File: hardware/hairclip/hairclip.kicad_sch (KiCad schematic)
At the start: 2 parts, among them U1 NRF52840-CKAA-R

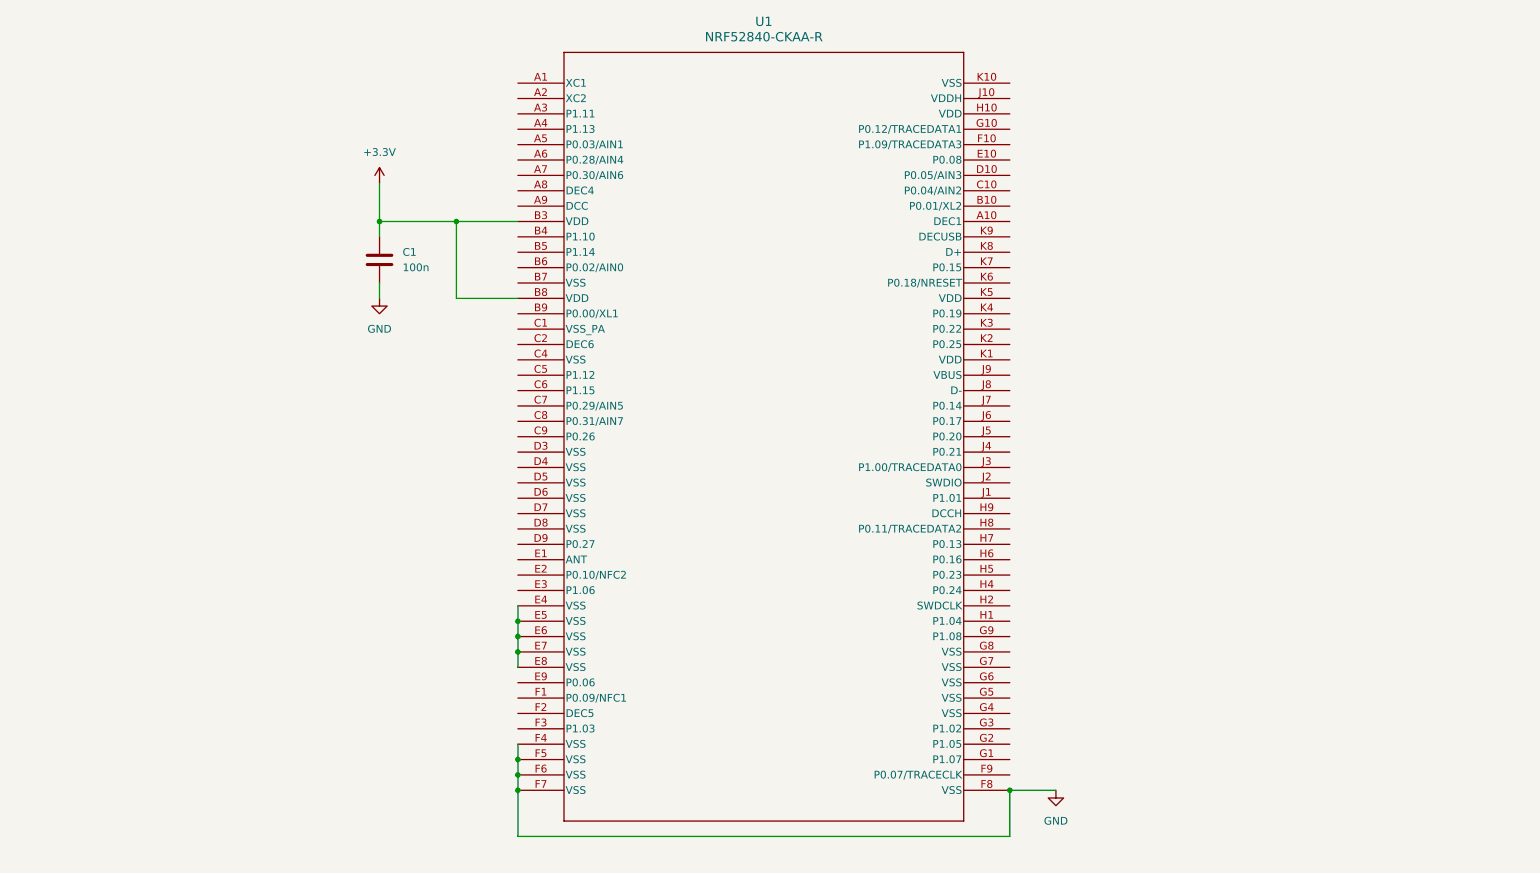
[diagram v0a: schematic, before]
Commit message: add low speed oscillator
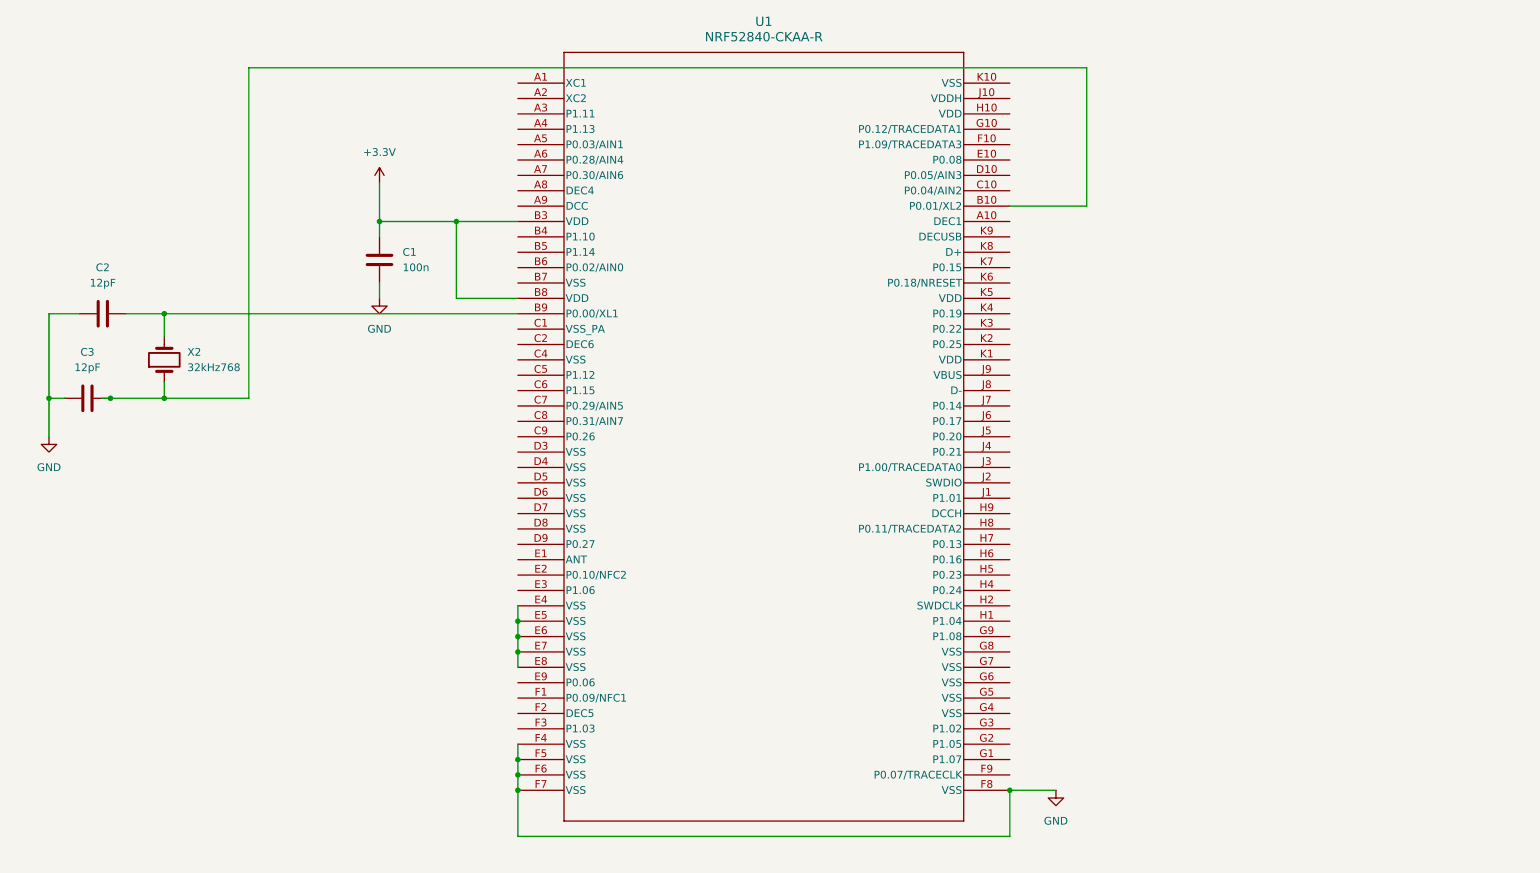
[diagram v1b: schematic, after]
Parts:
- added C2, C3: 12pF, symbol Device:C
- added X2: 32kHz768, symbol Device:Crystal
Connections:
- net GND: now also C2.1, C3.1
- net at U1.B10 (P0.01/XL2): now also C3.2, X2.1
- net at U1.B9 (P0.00/XL1): now also C2.2, X2.2

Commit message: Add high speed oscillator, antenna, LED, JTAG, Voltage regulator
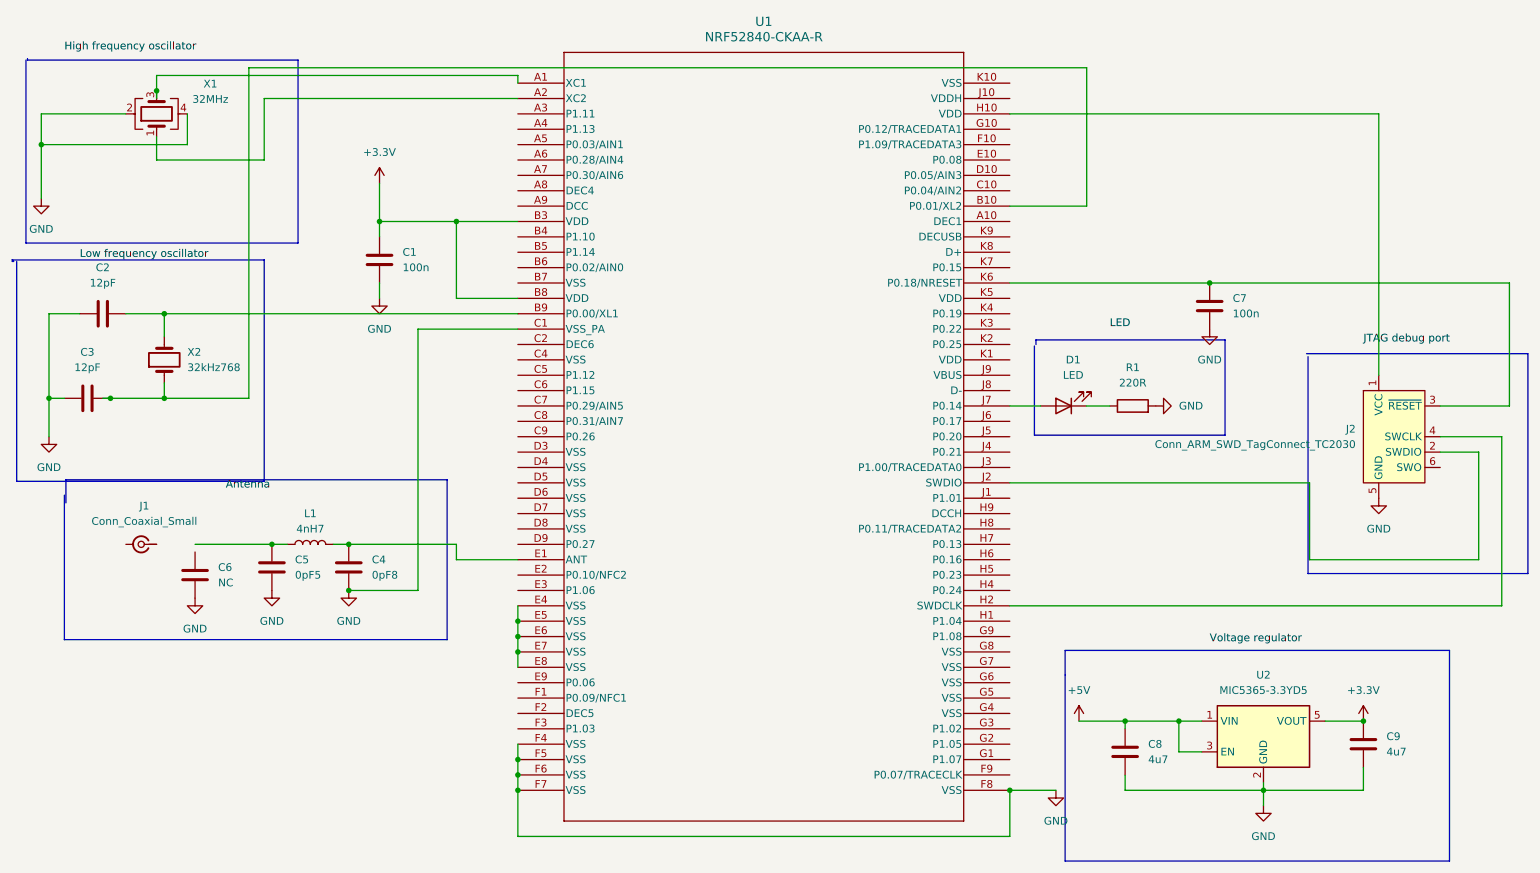
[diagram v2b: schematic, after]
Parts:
- added C4: 0pF8, symbol Device:C
- added C5: 0pF5, symbol Device:C
- added C6: NC, symbol Device:C
- added C7: 100n, symbol Device:C
- added C8, C9: 4u7, symbol Device:C
- added D1: LED, symbol Device:LED
- added J1: Conn_Coaxial_Small, symbol Connector:Conn_Coaxial_Small
- added J2: Conn_ARM_SWD_TagConnect_TC2030, Connector_PinHeader_1.27mm:PinHeader_2x05_P1.27mm_Vertical_SMD, symbol Connector:Conn_ARM_SWD_TagConnect_TC2030
- added L1: 4nH7, symbol Device:L
- added R1: 220R, symbol Device:R
- added U2: MIC5365-3.3YD5, Package_TO_SOT_SMD:SOT-23-5, symbol Regulator_Linear:MIC5365-3.3YD5
- added X1: 32MHz, symbol Device:Crystal_GND24
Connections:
- net +3.3V: now also C9.1, U2.5 (VOUT)
- net GND: now also U1.C1 (VSS_PA), C4.2, C5.2, C6.2, C7.2, C8.2, C9.2, J2.5 (GND), R1.2, U2.2 (GND), X1.2, X1.4
- net at U1.A1 (XC1): now also X1.3
- net at U1.A2 (XC2): now also X1.1
- net at U1.E1 (ANT): now also C4.1, L1.2
- net at U1.H10 (VDD): now also J2.1 (VCC)
- net at U1.H2 (SWDCLK): now also J2.4 (SWCLK)
- net at U1.J2 (SWDIO): now also J2.2 (SWDIO)
- net at U1.J7 (P0.14): now also D1.2 (A)
- net at U1.K6 (P0.18/NRESET): now also C7.1, J2.3 (~{RESET})
- new net: D1.1 (K), R1.1
- new net: C5.1, L1.1
- new net +5V: C8.1, U2.1 (VIN), U2.3 (EN)

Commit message: add initial pcb
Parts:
- C1: renamed from C3; footprint (none) -> Capacitor_SMD:C_0402_1005Metric
- C2: footprint (none) -> Capacitor_SMD:C_0402_1005Metric
- C3: renamed from C6; footprint (none) -> Capacitor_SMD:C_0402_1005Metric
- C4: renamed from C5; footprint (none) -> Capacitor_SMD:C_0402_1005Metric
- C5: renamed from C4; footprint (none) -> Capacitor_SMD:C_0402_1005Metric
- C6: renamed from C1; footprint (none) -> Capacitor_SMD:C_0402_1005Metric
- C7: renamed from C8; footprint (none) -> Capacitor_SMD:C_0805_2012Metric
- C8: renamed from C7; footprint (none) -> Capacitor_SMD:C_0402_1005Metric
- C9: footprint (none) -> Capacitor_SMD:C_0805_2012Metric
- D1: footprint (none) -> LED_SMD:LED_0201_0603Metric
- J1: footprint (none) -> Connector_Coaxial:U.FL_Hirose_U.FL-R-SMT-1_Vertical
- L1: footprint (none) -> Inductor_SMD:L_0402_1005Metric
- R1: footprint (none) -> Resistor_SMD:R_0402_1005Metric
- U1: footprint WLCSP94_3P5X3P6_NOR -> Package_DFN_QFN:Nordic_AQFN-73-1EP_7x7mm_P0.5mm
- X1, X2: footprint (none) -> Oscillator:Oscillator_SMD_Abracon_ASCO-4Pin_1.6x1.2mm
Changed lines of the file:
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@@
 		(dnp no)
 		(fields_autoplaced yes)
-		(property "Reference" "#PWR09"
+		(property "Reference" "#PWR014"
 			(at 241.3 116.84 0)
 			(effects
@@
 			(project "hairclip"
 				(path "/d641266f-28be-4124-8b00-4ae47c4ffb54"
-					(reference "#PWR09")
+					(reference "#PWR014")
 					(unit 1)
 				)
@@
 		(dnp no)
 		(fields_autoplaced yes)
-		(property "Reference" "#PWR06"
+		(property "Reference" "#PWR05"
 			(at 71.12 132.08 0)
 			(effects
@@
 			(project "hairclip"
 				(path "/d641266f-28be-4124-8b00-4ae47c4ffb54"
-					(reference "#PWR06")
+					(reference "#PWR05")
 					(unit 1)
 				)
@@
 		(dnp no)
 		(fields_autoplaced yes)
-		(property "Reference" "#PWR02"
+		(property "Reference" "#PWR07"
 			(at 76.2 83.82 0)
 			(effects
@@
 			(project "hairclip"
 				(path "/d641266f-28be-4124-8b00-4ae47c4ffb54"
-					(reference "#PWR02")
+					(reference "#PWR07")
 					(unit 1)
 				)
@@
 			)
 		)
-		(property "Footprint" ""
+		(property "Footprint" "Connector_Coaxial:U.FL_Hirose_U.FL-R-SMT-1_Vertical"
 			(at 36.83 118.11 0)
 			(effects
@@
 		(dnp no)
 		(fields_autoplaced yes)
-		(property "Reference" "C8"
+		(property "Reference" "C7"
 			(at 203.2 151.1299 0)
 			(effects
@@
 			)
 		)
-		(property "Footprint" ""
+		(property "Footprint" "Capacitor_SMD:C_0805_2012Metric"
 			(at 200.3552 156.21 0)
 			(effects
@@
 			(project "hairclip"
 				(path "/d641266f-28be-4124-8b00-4ae47c4ffb54"
-					(reference "C8")
+					(reference "C7")
 					(unit 1)
 				)
@@
 			)
 		)
-		(property "Footprint" "WLCSP94_3P5X3P6_NOR"
+		(property "Footprint" "Package_DFN_QFN:Nordic_AQFN-73-1EP_7x7mm_P0.5mm"
 			(at 99.06 41.91 0)
 			(effects
@@
 		(dnp no)
 		(fields_autoplaced yes)
-		(property "Reference" "C4"
+		(property "Reference" "C5"
 			(at 74.93 120.6499 0)
 			(effects
@@
 			)
 		)
-		(property "Footprint" ""
+		(property "Footprint" "Capacitor_SMD:C_0402_1005Metric"
 			(at 72.0852 125.73 0)
 			(effects
@@
 			(project "hairclip"
 				(path "/d641266f-28be-4124-8b00-4ae47c4ffb54"
-					(reference "C4")
+					(reference "C5")
 					(unit 1)
 				)
@@
 		(dnp no)
 		(fields_autoplaced yes)
-		(property "Reference" "C1"
+		(property "Reference" "C6"
 			(at 80.01 69.8499 0)
 			(effects
@@
 			)
 		)
-		(property "Footprint" ""
+		(property "Footprint" "Capacitor_SMD:C_0402_1005Metric"
 			(at 77.1652 74.93 0)
 			(effects
@@
 			(project "hairclip"
 				(path "/d641266f-28be-4124-8b00-4ae47c4ffb54"
-					(reference "C1")
+					(reference "C6")
 					(unit 1)
 				)
@@
 		(dnp no)
 		(fields_autoplaced yes)
-		(property "Reference" "C3"
+		(property "Reference" "C1"
 			(at 27.94 86.36 90)
 			(effects
@@
 			)
 		)
-		(property "Footprint" ""
+		(property "Footprint" "Capacitor_SMD:C_0402_1005Metric"
 			(at 31.75 93.0148 0)
 			(effects
@@
 			(project "hairclip"
 				(path "/d641266f-28be-4124-8b00-4ae47c4ffb54"
-					(reference "C3")
+					(reference "C1")
 					(unit 1)
 				)
@@
 			)
 		)
-		(property "Footprint" ""
+		(property "Footprint" "Capacitor_SMD:C_0402_1005Metric"
 			(at 34.29 79.0448 0)
 			(effects
@@
 		(dnp no)
 		(fields_autoplaced yes)
-		(property "Reference" "#PWR08"
+		(property "Reference" "#PWR03"
 			(at 45.72 133.35 0)
 			(effects
@@
 			(project "hairclip"
 				(path "/d641266f-28be-4124-8b00-4ae47c4ffb54"
-					(reference "#PWR08")
+					(reference "#PWR03")
 					(unit 1)
 				)
@@
 			)
 		)
-		(property "Footprint" ""
+		(property "Footprint" "LED_SMD:LED_0201_0603Metric"
 			(at 189.23 95.25 0)
 			(effects
@@
 		(dnp no)
 		(fields_autoplaced yes)
-		(property "Reference" "C5"
+		(property "Reference" "C4"
 			(at 62.23 120.6499 0)
 			(effects
@@
 			)
 		)
-		(property "Footprint" ""
+		(property "Footprint" "Capacitor_SMD:C_0402_1005Metric"
 			(at 59.3852 125.73 0)
 			(effects
@@
 			(project "hairclip"
 				(path "/d641266f-28be-4124-8b00-4ae47c4ffb54"
-					(reference "C5")
+					(reference "C4")
 					(unit 1)
 				)
@@
 			)
 		)
-		(property "Footprint" ""
+		(property "Footprint" "Oscillator:Oscillator_SMD_Abracon_ASCO-4Pin_1.6x1.2mm"
 			(at 39.37 46.99 0)
 			(effects
@@
 		(dnp no)
 		(fields_autoplaced yes)
-		(property "Reference" "#PWR010"
+		(property "Reference" "#PWR011"
 			(at 213.36 88.9 0)
 			(effects
@@
 			(project "hairclip"
 				(path "/d641266f-28be-4124-8b00-4ae47c4ffb54"
-					(reference "#PWR010")
+					(reference "#PWR011")
 					(unit 1)
 				)
@@
 			)
 		)
-		(property "Footprint" ""
+		(property "Footprint" "Resistor_SMD:R_0402_1005Metric"
 			(at 200.66 97.028 90)
 			(effects
@@
 		(dnp no)
 		(fields_autoplaced yes)
-		(property "Reference" "#PWR011"
+		(property "Reference" "#PWR012"
 			(at 222.25 167.64 0)
 			(effects
@@
 			(project "hairclip"
 				(path "/d641266f-28be-4124-8b00-4ae47c4ffb54"
-					(reference "#PWR011")
+					(reference "#PWR012")
 					(unit 1)
 				)
@@
 			)
 		)
-		(property "Footprint" ""
+		(property "Footprint" "Inductor_SMD:L_0402_1005Metric"
 			(at 64.77 118.11 0)
 			(effects
@@
 			)
 		)
-		(property "Footprint" ""
+		(property "Footprint" "Oscillator:Oscillator_SMD_Abracon_ASCO-4Pin_1.6x1.2mm"
 			(at 40.64 87.63 0)
 			(effects
@@
 		(dnp no)
 		(fields_autoplaced yes)
-		(property "Reference" "#PWR013"
+		(property "Reference" "#PWR09"
 			(at 191.77 151.13 0)
 			(effects
@@
 			(project "hairclip"
 				(path "/d641266f-28be-4124-8b00-4ae47c4ffb54"
-					(reference "#PWR013")
+					(reference "#PWR09")
 					(unit 1)
 				)
@@
 		(dnp no)
 		(fields_autoplaced yes)
-		(property "Reference" "#PWR07"
+		(property "Reference" "#PWR04"
 			(at 58.42 132.08 0)
 			(effects
@@
 			(project "hairclip"
 				(path "/d641266f-28be-4124-8b00-4ae47c4ffb54"
-					(reference "#PWR07")
+					(reference "#PWR04")
 					(unit 1)
 				)
@@
 		(dnp no)
 		(fields_autoplaced yes)
-		(property "Reference" "C7"
+		(property "Reference" "C8"
 			(at 217.17 77.4699 0)
 			(effects
@@
 			)
 		)
-		(property "Footprint" ""
+		(property "Footprint" "Capacitor_SMD:C_0402_1005Metric"
 			(at 214.3252 82.55 0)
 			(effects
@@
 			(project "hairclip"
 				(path "/d641266f-28be-4124-8b00-4ae47c4ffb54"
-					(reference "C7")
+					(reference "C8")
 					(unit 1)
 				)
@@
 		(dnp no)
 		(fields_autoplaced yes)
-		(property "Reference" "#PWR012"
+		(property "Reference" "#PWR013"
 			(at 238.76 151.13 0)
 			(effects
@@
 			(project "hairclip"
 				(path "/d641266f-28be-4124-8b00-4ae47c4ffb54"
-					(reference "#PWR012")
+					(reference "#PWR013")
 					(unit 1)
 				)
@@
 		(dnp no)
 		(fields_autoplaced yes)
-		(property "Reference" "#PWR014"
+		(property "Reference" "#PWR010"
 			(at 210.82 95.25 0)
 			(effects
@@
 			(project "hairclip"
 				(path "/d641266f-28be-4124-8b00-4ae47c4ffb54"
-					(reference "#PWR014")
+					(reference "#PWR010")
 					(unit 1)
 				)
@@
 		(dnp no)
 		(fields_autoplaced yes)
-		(property "Reference" "C6"
+		(property "Reference" "C3"
 			(at 49.53 121.9199 0)
 			(effects
@@
 			)
 		)
-		(property "Footprint" ""
+		(property "Footprint" "Capacitor_SMD:C_0402_1005Metric"
 			(at 46.6852 127 0)
 			(effects
@@
 			(project "hairclip"
 				(path "/d641266f-28be-4124-8b00-4ae47c4ffb54"
-					(reference "C6")
+					(reference "C3")
 					(unit 1)
 				)
@@
 		(dnp no)
 		(fields_autoplaced yes)
-		(property "Reference" "#PWR04"
+		(property "Reference" "#PWR02"
 			(at 21.59 106.68 0)
 			(effects
@@
 			(project "hairclip"
 				(path "/d641266f-28be-4124-8b00-4ae47c4ffb54"
-					(reference "#PWR04")
+					(reference "#PWR02")
 					(unit 1)
 				)
@@
 		(dnp no)
 		(fields_autoplaced yes)
-		(property "Reference" "#PWR01"
+		(property "Reference" "#PWR08"
 			(at 187.96 165.1 0)
 			(effects
@@
 			(project "hairclip"
 				(path "/d641266f-28be-4124-8b00-4ae47c4ffb54"
-					(reference "#PWR01")
+					(reference "#PWR08")
 					(unit 1)
 				)
@@
 			)
 		)
-		(property "Footprint" ""
+		(property "Footprint" "Capacitor_SMD:C_0805_2012Metric"
 			(at 239.7252 154.94 0)
 			(effects
@@
 		(dnp no)
 		(fields_autoplaced yes)
-		(property "Reference" "#PWR05"
+		(property "Reference" "#PWR01"
 			(at 20.32 67.31 0)
 			(effects
@@
 			(project "hairclip"
 				(path "/d641266f-28be-4124-8b00-4ae47c4ffb54"
-					(reference "#PWR05")
+					(reference "#PWR01")
 					(unit 1)
 				)
@@
 		(dnp no)
 		(fields_autoplaced yes)
-		(property "Reference" "#PWR03"
+		(property "Reference" "#PWR06"
 			(at 76.2 62.23 0)
 			(effects
@@
 			(project "hairclip"
 				(path "/d641266f-28be-4124-8b00-4ae47c4ffb54"
-					(reference "#PWR03")
-					(unit 1)
-				)
+					(reference "#PWR06")
+					(unit 1)
+				)
